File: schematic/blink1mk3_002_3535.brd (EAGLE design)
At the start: 14.9 x 9.6 mm, 15 parts, among them U1 EFM32HG309F64G, X2 USBPCB2

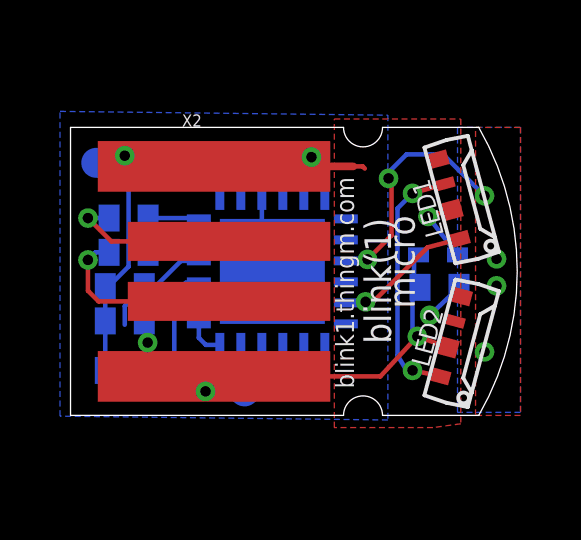
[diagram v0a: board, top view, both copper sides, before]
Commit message: added business card variant, and 3535 LED variant
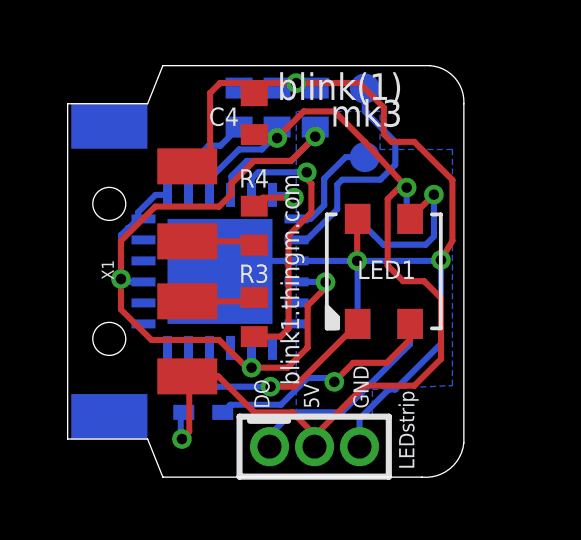
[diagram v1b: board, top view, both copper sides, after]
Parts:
- removed 5V, G: TPTP10R, testpad:TP10R
- removed X2: USBPCB2, todstuff:USB-A-PCB-2
- added JP3: M03MM, todstuff:1X03-1.5MM
- added X1: USB, todstuff:MOLEX-48037-1000
- LED1, LED2: value WS2812B4020SIDE -> WS2812B3535; device todstuff:SK6812-SIDE -> adafruit:LED3535
- moved C1 9.56 mm to (4.32, 5.46), turned to 90 degrees
- moved D1 9.42 mm to (3.17, -4.70)
- moved C3 8.74 mm to (5.59, 5.46), turned to 90 degrees
- moved C2 8.72 mm to (6.86, 5.46), turned to 90 degrees
- moved C4 8.43 mm to (4.83, 5.21), flipped to the top, turned to 90 degrees
- moved C 6.40 mm to (8.51, 3.81)
- moved R3 4.71 mm to (4.83, -1.52), flipped to the top, turned to 90 degrees
- moved D 4.64 mm to (8.51, 6.10)
- moved R4 4.20 mm to (4.83, 1.52), flipped to the top, turned to 270 degrees
- moved LED1 3.55 mm to (9.14, 0.00), turned to 90 degrees
- moved LED2 3.55 mm to (9.14, 0.00), flipped to the bottom, turned to 270 degrees
- moved U1 1.74 mm to (3.68, 0.00), turned to 90 degrees
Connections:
- net +5V: now also JP3.2, LED2.2, X1.1; no longer 5V.TP, LED2.1-VDD, X2.5V
- net DI: now also LED1.1; no longer LED1.4-DIN
- net DO: now also JP3.1, LED2.3; no longer LED2.2-DOUT
- net GND: now also JP3.3, LED1.4, LED2.4, X1.4; no longer G.TP, LED1.3-GND, LED2.3-GND, X2.GND
- net N$2: now also LED1.3, LED2.1; no longer LED1.2-DOUT, LED2.4-DIN
- net USB_D+: now also X1.3; no longer X2.USB_P
- net USB_D-: now also X1.2; no longer X2.USB_M
- net VLEDA: now also LED1.2; no longer LED1.1-VDD
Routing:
- net +3V3: track 6.94 -> 30.8 mm, vias 0 -> 4
- net GND: track 27.2 -> 39.5 mm
- net +5V: track 21.6 -> 33.4 mm
- net CAP0A: track 8.04 -> 0.00 mm, vias 6 -> 0
- net RUSB_D-: track 1.86 -> 9.31 mm, vias 0 -> 1
- net DO: track 0.00 -> 7.42 mm
- net DBG_SWDIO: track 1.25 -> 7.77 mm
- net VLEDA: track 2.43 -> 7.88 mm
- net USB_D-: track 6.68 -> 2.77 mm, vias 1 -> 0
- net USB_D+: track 5.73 -> 2.77 mm, vias 1 -> 0
- net N$2: track 8.42 -> 5.71 mm, vias 2 -> 1
- net DI: track 4.68 -> 7.39 mm
- net DBG_SWCLK: track 2.33 -> 4.18 mm
- net RUSB_D+: track 1.70 -> 2.22 mm, vias 0 -> 1
- added copper zone on layer 16, net GND
- removed copper zone on layer 16, net +3V3
- removed copper zone on layer 1, net CAP0A
- removed copper zone on layer 16, net CAP0A
- removed copper zone on layer 1, net GND
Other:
- board size 14.9 x 9.6 mm -> 13.2 x 13.7 mm
- board text added: "5V"
- board text added: "DO"
- board text added: "GND"
- board text added: "Gnd"
- board text added: "LEDstrip"
- board text added: "blink1mk3_002"
- board text added: "mk3"
- board text removed: "blink1mk3micro1"
- board text removed: "micro"
